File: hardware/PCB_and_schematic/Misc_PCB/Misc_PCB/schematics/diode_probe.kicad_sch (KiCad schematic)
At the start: 9 parts, among them J8 DIODE_BLINK_METER, Q10 BC817, Q9 BC817

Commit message: Add misc shift register for display schematic, ideal bridge and sd card switcher
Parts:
- J8: footprint (none) -> Connector_JST:JST_XH_B4B-XH-A_1x04_P2.50mm_Vertical
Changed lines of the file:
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@@
+				)
+			)
+			(project "Misc_PCB"
+				(path "/7b59bc46-701c-4caa-9db8-f0eec290561d/6babc747-648a-483d-982b-7a5f4e06013a"
+					(reference "#PWR018")
+					(unit 1)
 				)
 			)
@@
 			(project "Bidirectional_Power_Converter_24V-12V_with_BMS"
 				(path "/57ff2453-26d1-489b-aa83-9af273df178f/35ac2cba-a26f-48a2-8147-cc3c85b06bc6"
+					(reference "R16")
+					(unit 1)
+				)
+			)
+			(project "Misc_PCB"
+				(path "/7b59bc46-701c-4caa-9db8-f0eec290561d/6babc747-648a-483d-982b-7a5f4e06013a"
 					(reference "R16")
 					(unit 1)
@@
 			)
 		)
-		(property "Footprint" ""
+		(property "Footprint" "Connector_JST:JST_XH_B4B-XH-A_1x04_P2.50mm_Vertical"
 			(at 142.24 107.95 0)
 			(effects
@@
 				)
 			)
+			(project "Misc_PCB"
+				(path "/7b59bc46-701c-4caa-9db8-f0eec290561d/6babc747-648a-483d-982b-7a5f4e06013a"
+					(reference "J8")
+					(unit 1)
+				)
+			)
 		)
 	)
@@
 			(project "Bidirectional_Power_Converter_24V-12V_with_BMS"
 				(path "/57ff2453-26d1-489b-aa83-9af273df178f/35ac2cba-a26f-48a2-8147-cc3c85b06bc6"
+					(reference "#PWR023")
+					(unit 1)
+				)
+			)
+			(project "Misc_PCB"
+				(path "/7b59bc46-701c-4caa-9db8-f0eec290561d/6babc747-648a-483d-982b-7a5f4e06013a"
 					(reference "#PWR023")
 					(unit 1)
@@
 				)
 			)
+			(project "Misc_PCB"
+				(path "/7b59bc46-701c-4caa-9db8-f0eec290561d/6babc747-648a-483d-982b-7a5f4e06013a"
+					(reference "#PWR022")
+					(unit 1)
+				)
+			)
 		)
 	)
@@
 				)
 			)
+			(project "Misc_PCB"
+				(path "/7b59bc46-701c-4caa-9db8-f0eec290561d/6babc747-648a-483d-982b-7a5f4e06013a"
+					(reference "#PWR024")
+					(unit 1)
+				)
+			)
 		)
 	)
@@
 				)
 			)
+			(project "Misc_PCB"
+				(path "/7b59bc46-701c-4caa-9db8-f0eec290561d/6babc747-648a-483d-982b-7a5f4e06013a"
+					(reference "R19")
+					(unit 1)
+				)
+			)
 		)
 	)
@@
 			(project "Bidirectional_Power_Converter_24V-12V_with_BMS"
 				(path "/57ff2453-26d1-489b-aa83-9af273df178f/35ac2cba-a26f-48a2-8147-cc3c85b06bc6"
+					(reference "#PWR026")
+					(unit 1)
+				)
+			)
+			(project "Misc_PCB"
+				(path "/7b59bc46-701c-4caa-9db8-f0eec290561d/6babc747-648a-483d-982b-7a5f4e06013a"
 					(reference "#PWR026")
 					(unit 1)
@@
 				)
 			)
+			(project "Misc_PCB"
+				(path "/7b59bc46-701c-4caa-9db8-f0eec290561d/6babc747-648a-483d-982b-7a5f4e06013a"
+					(reference "#PWR027")
+					(unit 1)
+				)
+			)
 		)
 	)
@@
 				)
 			)
+			(project "Misc_PCB"
+				(path "/7b59bc46-701c-4caa-9db8-f0eec290561d/6babc747-648a-483d-982b-7a5f4e06013a"
+					(reference "R20")
+					(unit 1)
+				)
+			)
 		)
 	)
@@
 			(project "Bidirectional_Power_Converter_24V-12V_with_BMS"
 				(path "/57ff2453-26d1-489b-aa83-9af273df178f/35ac2cba-a26f-48a2-8147-cc3c85b06bc6"
+					(reference "D3")
+					(unit 1)
+				)
+			)
+			(project "Misc_PCB"
+				(path "/7b59bc46-701c-4caa-9db8-f0eec290561d/6babc747-648a-483d-982b-7a5f4e06013a"
 					(reference "D3")
 					(unit 1)
@@
 				)
 			)
+			(project "Misc_PCB"
+				(path "/7b59bc46-701c-4caa-9db8-f0eec290561d/6babc747-648a-483d-982b-7a5f4e06013a"
+					(reference "#PWR020")
+					(unit 1)
+				)
+			)
 		)
 	)
@@
 				)
 			)
+			(project "Misc_PCB"
+				(path "/7b59bc46-701c-4caa-9db8-f0eec290561d/6babc747-648a-483d-982b-7a5f4e06013a"
+					(reference "#PWR019")
+					(unit 1)
+				)
+			)
 		)
 	)
@@
 				)
 			)
+			(project "Misc_PCB"
+				(path "/7b59bc46-701c-4caa-9db8-f0eec290561d/6babc747-648a-483d-982b-7a5f4e06013a"
+					(reference "R18")
+					(unit 1)
+				)
+			)
 		)
 	)
@@
 				)
 			)
+			(project "Misc_PCB"
+				(path "/7b59bc46-701c-4caa-9db8-f0eec290561d/6babc747-648a-483d-982b-7a5f4e06013a"
+					(reference "Q10")
+					(unit 1)
+				)
+			)
 		)
 	)
@@
 				)
 			)
+			(project "Misc_PCB"
+				(path "/7b59bc46-701c-4caa-9db8-f0eec290561d/6babc747-648a-483d-982b-7a5f4e06013a"
+					(reference "Q9")
+					(unit 1)
+				)
+			)
 		)
 	)
@@
 				)
 			)
+			(project "Misc_PCB"
+				(path "/7b59bc46-701c-4caa-9db8-f0eec290561d/6babc747-648a-483d-982b-7a5f4e06013a"
+					(reference "D2")
+					(unit 1)
+				)
+			)
 		)
 	)
@@
 				)
 			)
+			(project "Misc_PCB"
+				(path "/7b59bc46-701c-4caa-9db8-f0eec290561d/6babc747-648a-483d-982b-7a5f4e06013a"
+					(reference "#PWR021")
+					(unit 1)
+				)
+			)
 		)
 	)
@@
 					(reference "#PWR025")
 					(unit 1)
+				)
+			)
+			(project "Misc_PCB"
+				(path "/7b59bc46-701c-4caa-9db8-f0eec290561d/6babc747-648a-483d-982b-7a5f4e06013a"
+					(reference "#PWR025")
+					(unit 1)

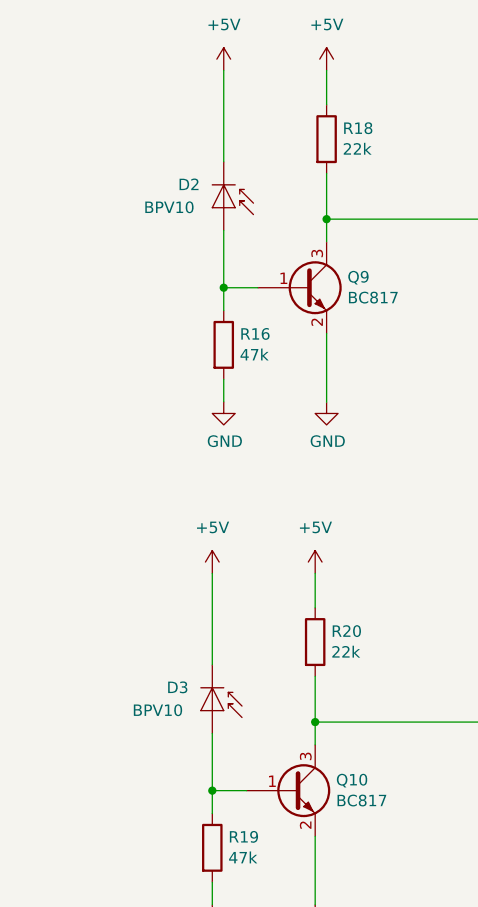
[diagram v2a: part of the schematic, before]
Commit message: Parts chage for bms
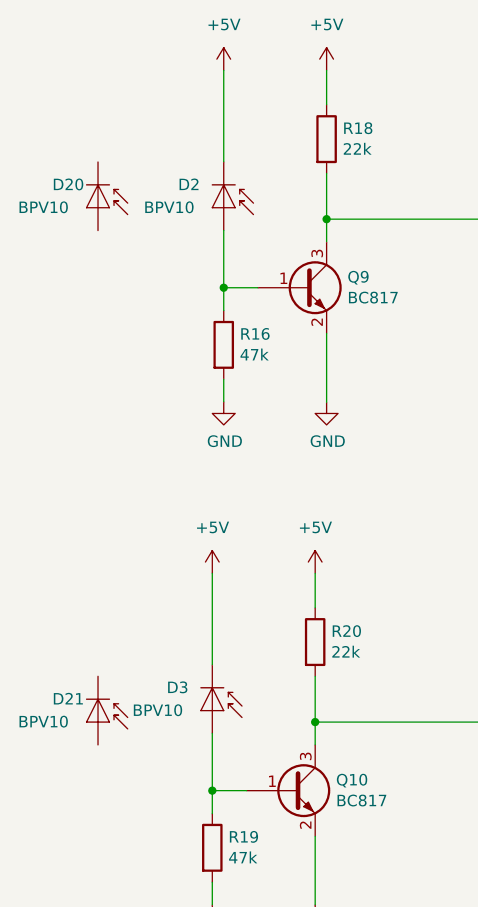
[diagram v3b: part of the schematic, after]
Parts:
- added D20, D21: BPV10, LED_THT:LED_D5.0mm, symbol Sensor_Optical:BP104
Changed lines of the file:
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@@
+	)
+	(symbol
+		(lib_id "Sensor_Optical:BP104")
+		(at 73.66 77.47 270)
+		(unit 1)
+		(exclude_from_sim no)
+		(in_bom yes)
+		(on_board yes)
+		(dnp no)
+		(property "Reference" "D20"
+			(at 68.58 74.93 90)
+			(effects
+				(font
+					(size 1.27 1.27)
+				)
+				(justify left)
+			)
+		)
+		(property "Value" "BPV10"
+			(at 64.77 77.47 90)
+			(effects
+				(font
+					(size 1.27 1.27)
+				)
+				(justify left)
+			)
+		)
+		(property "Footprint" "LED_THT:LED_D5.0mm"
+			(at 78.105 77.47 0)
+			(effects
+				(font
+					(size 1.27 1.27)
+				)
+				(hide yes)
+			)
+		)
+		(property "Datasheet" "https://www.vishay.com/docs/81502/bpv10.pdf"
+			(at 73.66 76.2 0)
+			(effects
+				(font
+					(size 1.27 1.27)
+				)
+				(hide yes)
+			)
+		)
+		(property "Description" ""
+			(at 73.66 77.47 0)
+			(effects
+				(font
+					(size 1.27 1.27)
+				)
+				(hide yes)
+			)
+		)
+		(pin "1"
+		)
+		(pin "2"
+		)
+		(instances
+			(project "Misc_PCB"
+				(path "/7b59bc46-701c-4caa-9db8-f0eec290561d/6babc747-648a-483d-982b-7a5f4e06013a"
+					(reference "D20")
+					(unit 1)
+				)
+			)
+		)
 	)
 	(symbol
@@
 					(unit 1)
 				)
+			)
+		)
+	)
+	(symbol
+		(lib_id "Sensor_Optical:BP104")
+		(at 73.66 134.62 270)
+		(unit 1)
+		(exclude_from_sim no)
+		(in_bom yes)
+		(on_board yes)
+		(dnp no)
+		(property "Reference" "D21"
+			(at 68.58 132.08 90)
+			(effects
+				(font
+					(size 1.27 1.27)
+				)
+				(justify left)
+			)
+		)
+		(property "Value" "BPV10"
+			(at 64.77 134.62 90)
+			(effects
+				(font
+					(size 1.27 1.27)
+				)
+				(justify left)
+			)
+		)
+		(property "Footprint" "LED_THT:LED_D5.0mm"
+			(at 78.105 134.62 0)
+			(effects
+				(font
+					(size 1.27 1.27)
+				)
+				(hide yes)
+			)
+		)
+		(property "Datasheet" "https://www.vishay.com/docs/81502/bpv10.pdf"
+			(at 73.66 133.35 0)
+			(effects
+				(font
+					(size 1.27 1.27)
+				)
+				(hide yes)
+			)
+		)
+		(property "Description" ""
+			(at 73.66 134.62 0)
+			(effects
+				(font
+					(size 1.27 1.27)
+				)
+				(hide yes)
+			)
+		)
+		(pin "1"
+		)
+		(pin "2"
+		)
+		(instances
+			(project "Misc_PCB"
+				(path "/7b59bc46-701c-4caa-9db8-f0eec290561d/6babc747-648a-483d-982b-7a5f4e06013a"
+					(reference "D21")
+					(unit 1)
+				)

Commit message: power tracking heater progress
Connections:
- net +5V: now also D20.1 (K), D21.1 (K)
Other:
- moved on the sheet: D21
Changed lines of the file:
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@@
 	(paper "A4")
+	(junction
+		(at 87.63 64.77)
+		(diameter 0)
+		(color 0 0 0 0)
+	)
+	(junction
+		(at 86.36 121.92)
+		(diameter 0)
+		(color 0 0 0 0)
+	)
 	(junction
 		(at 97.79 134.62)
@@
 	(wire
 		(pts
-			(xy 86.36 128.27) (xy 86.36 118.11)
+			(xy 86.36 128.27) (xy 86.36 121.92)
 		)
 		(stroke
@@
 	(wire
 		(pts
-			(xy 87.63 72.39) (xy 87.63 62.23)
+			(xy 87.63 64.77) (xy 73.66 64.77)
+		)
+		(stroke
+			(width 0)
+			(type default)
+		)
+	)
+	(wire
+		(pts
+			(xy 87.63 72.39) (xy 87.63 64.77)
 		)
 		(stroke
@@
 	(wire
 		(pts
+			(xy 86.36 121.92) (xy 73.66 121.92)
+		)
+		(stroke
+			(width 0)
+			(type default)
+		)
+	)
+	(wire
+		(pts
 			(xy 86.36 152.4) (xy 86.36 154.94)
 		)
@@
 	(wire
 		(pts
+			(xy 73.66 121.92) (xy 73.66 128.27)
+		)
+		(stroke
+			(width 0)
+			(type default)
+		)
+	)
+	(wire
+		(pts
 			(xy 99.06 62.23) (xy 99.06 66.04)
 		)
@@
 	(wire
 		(pts
+			(xy 87.63 64.77) (xy 87.63 62.23)
+		)
+		(stroke
+			(width 0)
+			(type default)
+		)
+	)
+	(wire
+		(pts
 			(xy 137.16 107.95) (xy 129.54 107.95)
 		)
@@
 	(wire
 		(pts
+			(xy 86.36 121.92) (xy 86.36 118.11)
+		)
+		(stroke
+			(width 0)
+			(type default)
+		)
+	)
+	(wire
+		(pts
 			(xy 99.06 73.66) (xy 99.06 78.74)
 		)
@@
 		(pts
 			(xy 90.17 142.24) (xy 86.36 142.24)
+		)
+		(stroke
+			(width 0)
+			(type default)
+		)
+	)
+	(wire
+		(pts
+			(xy 73.66 64.77) (xy 73.66 72.39)
 		)
 		(stroke
@@
 	(symbol
 		(lib_id "Sensor_Optical:BP104")
-		(at 73.66 134.62 270)
+		(at 73.66 133.35 270)
 		(unit 1)
 		(exclude_from_sim no)
@@
 		(dnp no)
 		(property "Reference" "D21"
-			(at 68.58 132.08 90)
+			(at 68.58 130.81 90)
 			(effects
 				(font
@@
 		)
 		(property "Value" "BPV10"
-			(at 64.77 134.62 90)
+			(at 64.77 133.35 90)
 			(effects
 				(font
@@
 		)
 		(property "Footprint" "LED_THT:LED_D5.0mm"
-			(at 78.105 134.62 0)
+			(at 78.105 133.35 0)
 			(effects
 				(font
@@
 		)
 		(property "Datasheet" "https://www.vishay.com/docs/81502/bpv10.pdf"
+			(at 73.66 132.08 0)
+			(effects
+				(font
+					(size 1.27 1.27)
+				)
+				(hide yes)
+			)
+		)
+		(property "Description" ""
 			(at 73.66 133.35 0)
 			(effects
 				(font
-					(size 1.27 1.27)
-				)
-				(hide yes)
-			)
-		)
-		(property "Description" ""
-			(at 73.66 134.62 0)
-			(effects
-				(font

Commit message: kicad oc
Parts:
- added J13: DIODE_BLINK_METER, Connector_JST:JST_XH_B4B-XH-A_1x04_P2.50mm_Vertical, symbol Connector_Generic:Conn_01x04
- added Q13, Q14: BC817, Package_TO_SOT_SMD:SOT-23, symbol Transistor_BJT:BC817
- added R48, R49: 47k, Resistor_SMD:R_0805_2012Metric_Pad1.20x1.40mm_HandSolder, symbol Device:R
- added R50, R51: 22k, Resistor_SMD:R_0805_2012Metric_Pad1.20x1.40mm_HandSolder, symbol Device:R
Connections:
- net +5V: now also J13.1 (Pin_1), R50.1, R51.1
- net GND: now also J13.4 (Pin_4), Q13.2 (E), Q14.2 (E), R48.2, R49.2
- net at D20.2 (A): now also Q13.1 (B), R48.1
- net at D21.2 (A): now also Q14.1 (B), R49.1
- new net: J13.3 (Pin_3), Q13.3 (C), R50.2
- new net: J13.2 (Pin_2), Q14.3 (C), R51.2
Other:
- moved on the sheet: D20, D21

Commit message: done LT3652
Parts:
- J13: value DIODE_BLINK_METER -> DIODE_BLINK_METER_OUT; footprint Connector_JST:JST_XH_B4B-XH-A_1x04_P2.50mm_Vertical -> Connector_PinHeader_2.54mm:PinHeader_1x04_P2.54mm_Vertical
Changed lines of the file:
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@@
 			)
 		)
-		(property "Value" "DIODE_BLINK_METER"
+		(property "Value" "DIODE_BLINK_METER_OUT"
 			(at 177.8 102.8701 0)
 			(effects
@@
 			)
 		)
-		(property "Footprint" "Connector_JST:JST_XH_B4B-XH-A_1x04_P2.50mm_Vertical"
+		(property "Footprint" "Connector_PinHeader_2.54mm:PinHeader_1x04_P2.54mm_Vertical"
 			(at 180.34 105.41 0)
 			(effects
